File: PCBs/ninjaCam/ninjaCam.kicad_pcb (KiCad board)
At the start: 2 copper layers, 84.2 x 52.2 mm, 16 parts, among them J1 DVI-HX-107DIP

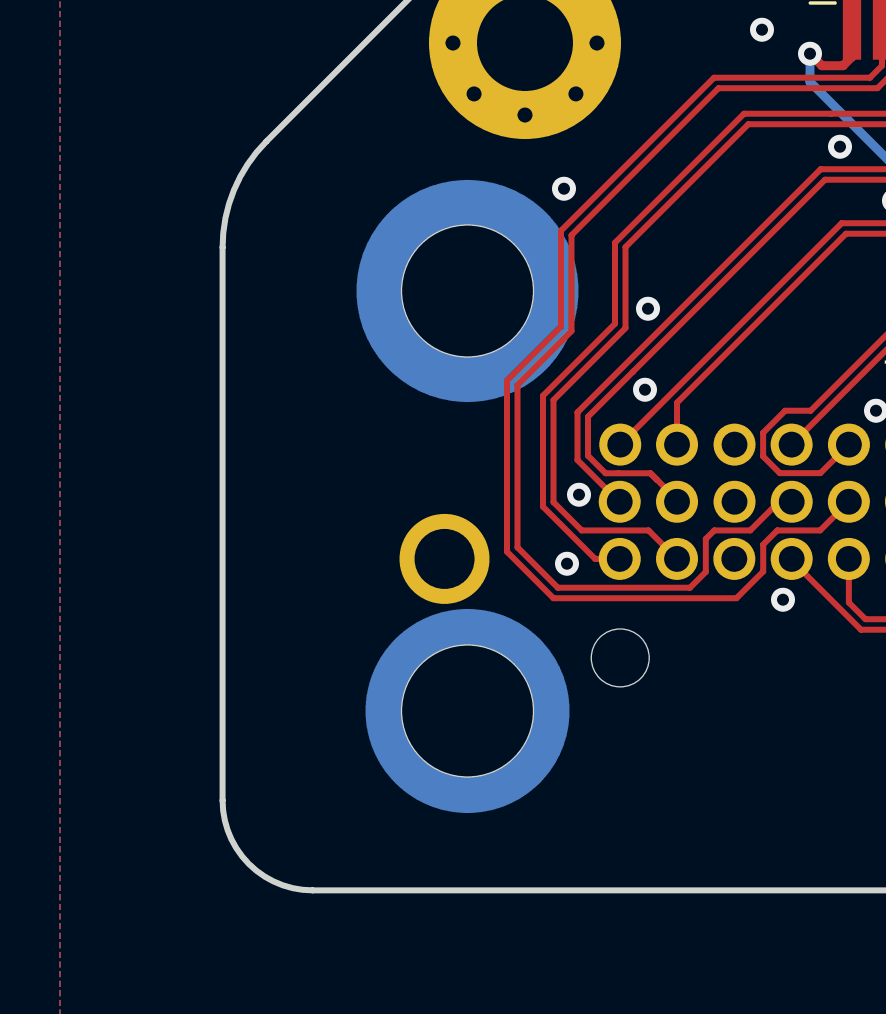
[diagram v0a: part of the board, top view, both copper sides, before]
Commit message: moved one pair of mounting holes (for cam holder) to be x=50mm y=10mm relative to other cam holder mounting hole
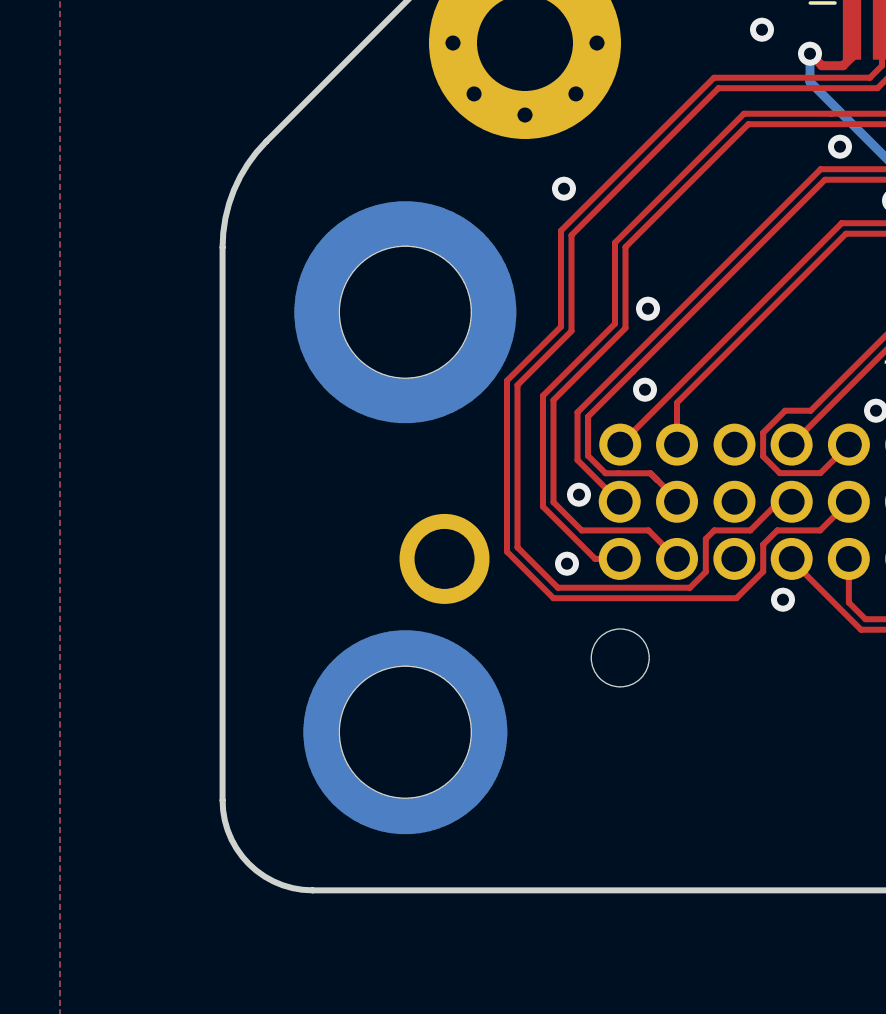
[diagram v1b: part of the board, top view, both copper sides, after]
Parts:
- moved H1 2.19 mm to (199.6, 128.4)
- moved H12 2.19 mm to (199.6, 142.4)
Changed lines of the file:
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@@
   )
   (footprint "Eagle_WA-SMSI (rev21a):WA-SMSI_9774010360" (layer "B.Cu")
-    (at 201.684179 141.709222 180)
+    (at 199.611179 142.416222 180)
     (descr "<B>WA-SMSI SMT Steel Spacer, M3 Thread Internal\n<BR></B>Thread Internal M3\n<BR>Height = 1mm")
     (property "Sheetfile" "ninjaCam.kicad_sch")
@@
   )
   (footprint "Eagle_WA-SMSI (rev21a):WA-SMSI_9774010360" (layer "B.Cu")
-    (at 201.684179 127.709222 180)
+    (at 199.611179 128.416222 180)
     (descr "<B>WA-SMSI SMT Steel Spacer, M3 Thread Internal\n<BR></B>Thread Internal M3\n<BR>Height = 1mm")
     (property "Sheetfile" "ninjaCam.kicad_sch")
